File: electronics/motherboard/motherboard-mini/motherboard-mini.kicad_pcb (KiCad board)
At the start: 2 copper layers, 57.7 x 102.2 mm, 76 parts, among them J1 TBP02R2-381-03BE, J2 TBP02R2-381-02BE, J3 ST1W008S4AR1500, J4 TBP02R2-381-03BE, J5 USB4070-30-C_REVC5, J6 CONUFL001-SMD-T, J7 21992304, J8 Conn_01x04_Male, J9 TBP02R2-381-02BE, Q1 BSS214NW, Q2 AOD417, U1 MCP73832-2-OT, U2 NCP718xSN500, U3 INA219BxD, U4 LT3652IMSE, U6 INA219BxD, U7 LD39015M33R, U8 MIC2145BMM, U9 RFM95W-915S2

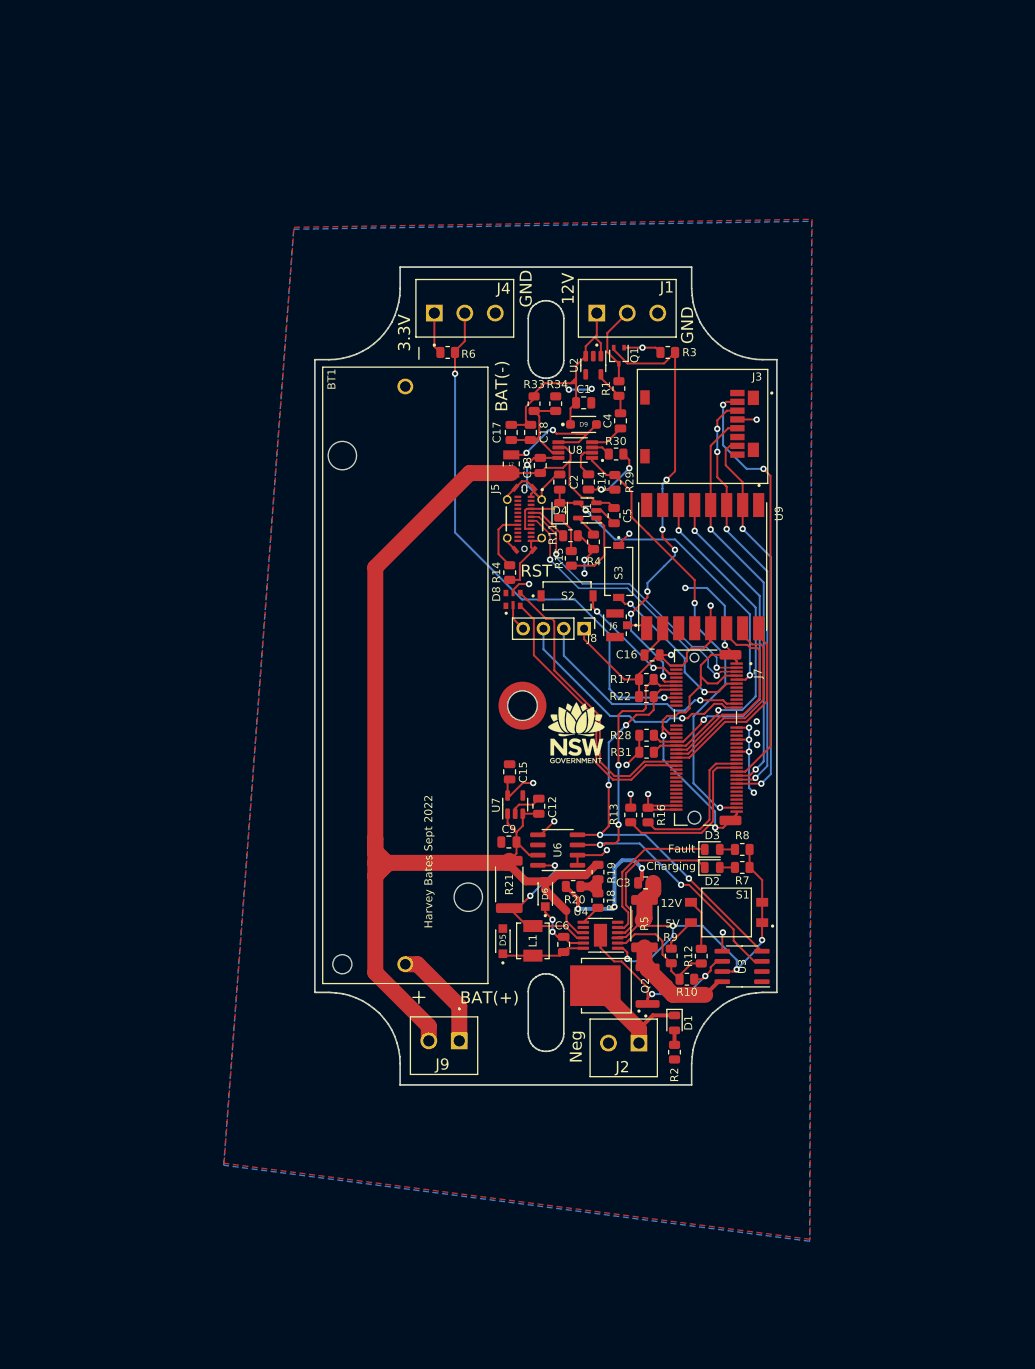
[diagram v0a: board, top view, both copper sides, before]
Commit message: realign with master branch before kangaroo board is split into seperate repo
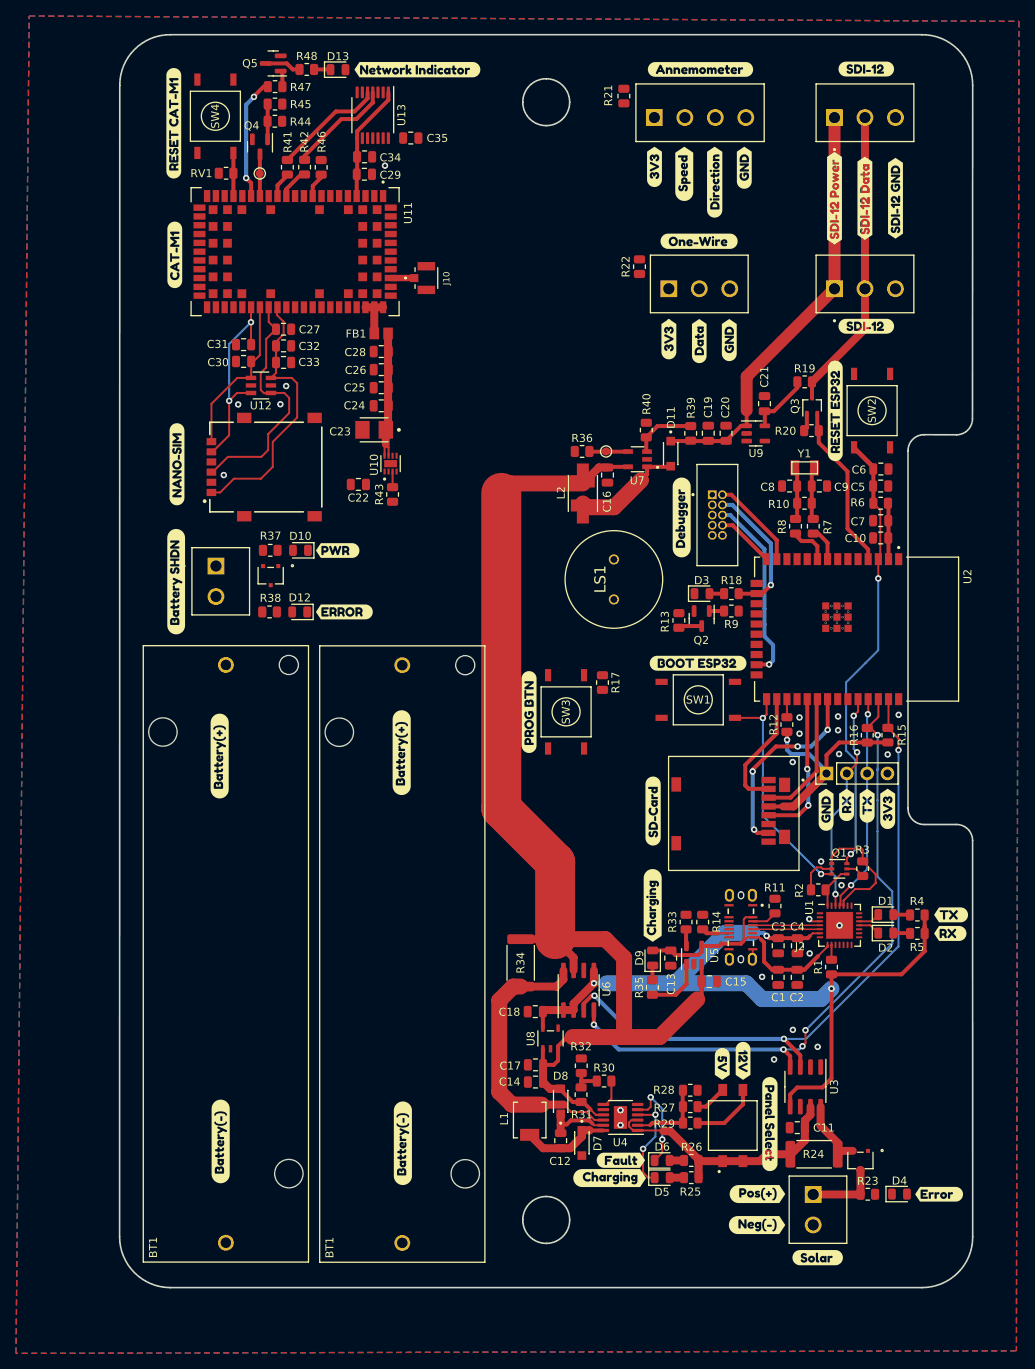
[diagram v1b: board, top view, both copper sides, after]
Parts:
- removed the BT1 at (67.7, 106.8)
- removed MP1: 9774025151R, 9774025151R:WE_9774025151R
- removed S2: RST, PTS636_SM43J_SMTR_LFS:SW_PTS636_SM43J_SMTR_LFS
- removed S3: BOOT, PTS636_SM43J_SMTR_LFS:SW_PTS636_SM43J_SMTR_LFS
- added BT1: 1043, 1043:BAT_1043, F.Cu at (45.3, 141.6)
- added BT1: 1043, 1043:BAT_1043, F.Cu at (67.3, 141.6)
- added C10: 22uF, Capacitor_SMD:C_0805_2012Metric, F.Cu at (127.1, 89.6)
- added C11: 10uF, Capacitor_SMD:C_0805_2012Metric, F.Cu at (116.7, 163.3)
- added C19: 10uF, Capacitor_SMD:C_0805_2012Metric, F.Cu at (105.6, 76.5)
- added C20: 1uF, Capacitor_SMD:C_0805_2012Metric, F.Cu at (107.8, 76.5)
- added C21: 1uF, Capacitor_SMD:C_0805_2012Metric, F.Cu at (112.6, 72.8)
- added C22: 1uF, Capacitor_SMD:C_0805_2012Metric, F.Cu at (61.8, 82.9)
- added C23: 100uF, T520B107M006ATE015:CAPPM3528X210N, F.Cu at (63.8, 76.1)
- added C24: 100nF, Capacitor_SMD:C_0805_2012Metric, F.Cu at (64.7, 73.1)
- added C25: 10nF, Capacitor_SMD:C_0805_2012Metric, F.Cu at (64.7, 70.8)
- added C26: 15pF, Capacitor_SMD:C_0805_2012Metric, F.Cu at (64.7, 68.5)
- added C27: 47pF, Capacitor_SMD:C_0805_2012Metric, F.Cu at (52.5, 63.5)
- added C28: 68pF, Capacitor_SMD:C_0805_2012Metric, F.Cu at (64.7, 66.3)
- added C29: 100nF, Capacitor_SMD:C_0805_2012Metric, F.Cu at (62.6, 44.1)
- added C30: 47pF, Capacitor_SMD:C_0805_2012Metric, F.Cu at (47.5, 67.5)
- added C31: 47pF, Capacitor_SMD:C_0805_2012Metric, F.Cu at (47.5, 65.4)
- added C32: 47pF, Capacitor_SMD:C_0805_2012Metric, F.Cu at (52.5, 65.6)
- added C33: 100nF, Capacitor_SMD:C_0805_2012Metric, F.Cu at (52.5, 67.7)
- added C34: 0.1uF, Capacitor_SMD:C_0805_2012Metric, F.Cu at (62.6, 42.0)
- added C35: 0.1uF, Capacitor_SMD:C_0805_2012Metric, F.Cu at (68.4, 39.6)
- added C7: 0.1uF, Capacitor_SMD:C_0805_2012Metric, F.Cu at (127.1, 87.4)
- added C8: 12pF, Capacitor_SMD:C_0805_2012Metric, F.Cu at (115.7, 83.1)
- added D10: LED(Green), LED_SMD:LED_0805_2012Metric, F.Cu at (54.6, 91.1)
- added D11: SS34LW_RVG, SS34LW_RVG:SODFL3718X102N, F.Cu at (100.9, 79.0)
- added D12: LED(Red), LED_SMD:LED_0805_2012Metric, F.Cu at (54.5, 98.8)
- added D13: LED, LED_SMD:LED_0805_2012Metric, F.Cu at (59.3, 31.1)
- added D7: SS34LW_RVG, SS34LW_RVG:SODFL3718X102N, F.Cu at (89.8, 165.2)
- added FB1: FBMH2012HM221-TV, FBMH2012HM221-TV:BEADC2012X105N, F.Cu at (64.7, 64.0)
- added J10: CONUFL001-SMD-T, CONUFL001-SMD-T:LINX_CONUFL001-SMD-T, F.Cu at (70.3, 57.1)
- added J11: SIM8060-6-0-14-00-A, SIM8060-6-0-14-00-A:GCT_SIM8060-6-0-14-00-A, F.Cu at (50.3, 80.7)
- added J12: JTAG, 3221-10-0100-00:CNC_3221-10-0100-00, F.Cu at (106.7, 86.7)
- added LS1: PS1240P02BT, PS1240P02BT:XDCR_PS1240P02BT, F.Cu at (93.8, 94.8)
- added MOSFET1: SSM3J340R_LF, SSM3J340R_LF:SSM3J340R_LF, F.Cu at (124.6, 167.4)
- added MOSFET2: SSM3J340R_LF, SSM3J340R_LF:SSM3J340R_LF, F.Cu at (50.9, 94.3)
- added Q3: BSS214NW, Package_TO_SOT_SMD:SOT-323_SC-70, F.Cu at (118.5, 73.0)
- added Q4: BC847, Package_TO_SOT_SMD:SOT-23, F.Cu at (49.5, 40.7)
- added Q5: BC847, Package_TO_SOT_SMD:SOT-23, F.Cu at (51.2, 30.3)
- added R23: 4.7K, Resistor_SMD:R_0805_2012Metric, F.Cu at (125.5, 171.6)
- added R24: 0.1, Resistor_SMD:R_2512_6332Metric, F.Cu at (118.8, 166.6)
- added R25: 4.7K, Resistor_SMD:R_0805_2012Metric, F.Cu at (103.5, 169.6)
- added R26: 4.7K, Resistor_SMD:R_0805_2012Metric, F.Cu at (103.5, 167.4)
- added R27: 23K, Resistor_SMD:R_0805_2012Metric, F.Cu at (103.3, 160.7)
- added R32: 330K, Resistor_SMD:R_0805_2012Metric, F.Cu at (89.7, 155.6)
- added R35: 1K, Resistor_SMD:R_0805_2012Metric, F.Cu at (98.6, 145.8)
- added R36: 100K, Resistor_SMD:R_0805_2012Metric, F.Cu at (89.8, 78.8)
- added R37: 4.7K, Resistor_SMD:R_0805_2012Metric, F.Cu at (50.8, 91.1)
- added R38: 4.7K, Resistor_SMD:R_0805_2012Metric, F.Cu at (50.7, 98.8)
- added R39: 43.3K, Resistor_SMD:R_0805_2012Metric, F.Cu at (103.4, 76.5)
- added R40: 5K, Resistor_SMD:R_0805_2012Metric, F.Cu at (97.8, 76.1)
- added R41: 0, Resistor_SMD:R_0805_2012Metric, F.Cu at (53.0, 43.2)
- added R42: 0, Resistor_SMD:R_0805_2012Metric, F.Cu at (55.1, 43.2)
- added R43: 100K, Resistor_SMD:R_0805_2012Metric, F.Cu at (66.1, 84.2)
- added R44: 10K, Resistor_SMD:R_0805_2012Metric, F.Cu at (51.4, 37.5)
- added R45: 47K, Resistor_SMD:R_0805_2012Metric, F.Cu at (51.4, 35.4)
- added R46: 0, Resistor_SMD:R_0805_2012Metric, F.Cu at (57.2, 43.3)
- added R47: 10K, Resistor_SMD:R_0805_2012Metric, F.Cu at (51.4, 33.2)
- added R48: 1.2K, Resistor_SMD:R_0805_2012Metric, F.Cu at (55.4, 31.0)
- added RV1: ESD_RST_IN, Resistor_SMD:R_0805_2012Metric, F.Cu at (45.3, 44.0)
- added SW1: BOOT, 1977223-6:1977223-6, F.Cu at (104.3, 109.8)
- added SW2: RESET, 1977223-6:1977223-6, F.Cu at (126.1, 73.7)
- added SW3: PROG_BTN, 1977223-6:1977223-6, F.Cu at (87.8, 111.3)
- added SW4: CAT_M1_RST, 1977223-6:1977223-6, F.Cu at (44.0, 36.9)
- added TP1: 12V_EN, TestPoint:TestPoint_Pad_D1.0mm, F.Cu at (92.8, 78.8)
- added TP4: PWR_ON, TestPoint:TestPoint_Pad_D1.0mm, F.Cu at (49.5, 44.0)
- added U10: TPS22967DSGR, TPS22967DSGR:SON50P200X200X80-9N, F.Cu at (65.9, 80.3)
- added U11: SARA-R410M-02B, SARA-R410M-02B:XCVR_SARA-R410M-02B, F.Cu at (53.9, 53.8)
- added U12: AOZ8904CIL, AOZ8904CIL:AOZ8904CIL, F.Cu at (49.7, 70.5)
- added U13: TXB0104PW, Package_SO:TSSOP-14_4.4x5mm_P0.65mm, F.Cu at (63.6, 36.8)
- added U5: MCP73832-2-OT, Package_TO_SOT_SMD:SOT-23-5, F.Cu at (103.8, 141.7)
- added Y1: 32.768KHz, ABS07AIG-32:XTAL320X150X90, F.Cu at (117.6, 80.8)
- added kibuzzard-635F8A2B: G***, kibuzzard-635F8A2B, F.Cu at (122.9, 123.0)
- added kibuzzard-635F8A68: G***, kibuzzard-635F8A68, F.Cu at (125.4, 123.1)
- added kibuzzard-635F8A75: G***, kibuzzard-635F8A75, F.Cu at (128.0, 123.5)
- added kibuzzard-635F8A8D: G***, kibuzzard-635F8A8D, F.Cu at (120.3, 123.6)
- added kibuzzard-635F8E2B: G***, kibuzzard-635F8E2B, F.Cu at (44.6, 165.0)
- added kibuzzard-635F8E2B: G***, kibuzzard-635F8E2B, F.Cu at (67.4, 165.2)
- added kibuzzard-635F8E59: G***, kibuzzard-635F8E59, F.Cu at (67.2, 116.4)
- added kibuzzard-635F8E59: G***, kibuzzard-635F8E59, F.Cu at (44.5, 116.8)
- added kibuzzard-635F905F: G***, kibuzzard-635F905F, F.Cu at (60.1, 98.8)
- added kibuzzard-635F906F: G***, kibuzzard-635F906F, F.Cu at (59.3, 91.2)
- added kibuzzard-635F91A1: G***, kibuzzard-635F91A1, F.Cu at (135.9, 136.7)
- added kibuzzard-635F91AE: G***, kibuzzard-635F91AE, F.Cu at (135.8, 139.0)
- added kibuzzard-635F9520: G***, kibuzzard-635F9520, F.Cu at (39.2, 80.4)
- added kibuzzard-635F9541: G***, kibuzzard-635F9541, F.Cu at (39.1, 95.0)
- added kibuzzard-635FAFDC: G***, kibuzzard-635FAFDC, F.Cu at (69.2, 31.1)
- added kibuzzard-635FB008: G***, kibuzzard-635FB008, F.Cu at (38.8, 37.8)
- added kibuzzard-635FB066: G***, kibuzzard-635FB066, F.Cu at (38.9, 54.2)
- added kibuzzard-635FB58D: G***, kibuzzard-635FB58D, F.Cu at (121.5, 73.7)
- added kibuzzard-635FB5EA: G***, kibuzzard-635FB5EA, F.Cu at (104.3, 105.2)
- added kibuzzard-63606B27: G***, kibuzzard-63606B27, F.Cu at (119.2, 179.6)
- added kibuzzard-63606B50: G***, kibuzzard-63606B50, F.Cu at (111.7, 171.6)
- added kibuzzard-63606B62: G***, kibuzzard-63606B62, F.Cu at (111.7, 175.5)
- added kibuzzard-63606B90: G***, kibuzzard-63606B90, F.Cu at (107.3, 155.3)
- added kibuzzard-63606BA0: G***, kibuzzard-63606BA0, F.Cu at (109.9, 154.9)
- added kibuzzard-63606BEB: G***, kibuzzard-63606BEB, F.Cu at (113.3, 162.8)
- added kibuzzard-63606C19: G***, kibuzzard-63606C19, F.Cu at (134.4, 171.6)
- added kibuzzard-63606D76: G***, kibuzzard-63606D76, F.Cu at (93.2, 169.6)
- added kibuzzard-63606D99: G***, kibuzzard-63606D99, F.Cu at (94.7, 167.4)
- added kibuzzard-6360750E: G***, kibuzzard-6360750E, F.Cu at (98.6, 135.5)
- added kibuzzard-636098FD: G***, kibuzzard-636098FD, F.Cu at (98.7, 123.7)
- added kibuzzard-6360A408: G***, kibuzzard-6360A408, F.Cu at (83.2, 111.3)
- added kibuzzard-6360A96B: G***, kibuzzard-6360A96B, F.Cu at (125.3, 63.1)
- added kibuzzard-6360A96B: G***, kibuzzard-6360A96B, F.Cu at (125.3, 31.0)
- added kibuzzard-6360B45A: G***, kibuzzard-6360B45A, F.Cu at (102.2, 87.0)
- added kibuzzard-6360B4B7: G***, kibuzzard-6360B4B7, F.Cu at (125.2, 47.1)
- added kibuzzard-6360B4C0: G***, kibuzzard-6360B4C0, F.Cu at (121.3, 47.1)
- added kibuzzard-6360B4D6: G***, kibuzzard-6360B4D6, F.Cu at (129.0, 47.1)
- added kibuzzard-6360B5B2: G***, kibuzzard-6360B5B2, F.Cu at (104.6, 31.0)
- added kibuzzard-6360B5D7: G***, kibuzzard-6360B5D7, F.Cu at (100.7, 64.7)
- added kibuzzard-6360B5D7: G***, kibuzzard-6360B5D7, F.Cu at (98.8, 43.2)
- added kibuzzard-6360B5FD: G***, kibuzzard-6360B5FD, F.Cu at (102.6, 44.1)
- added kibuzzard-6360B60D: G***, kibuzzard-6360B60D, F.Cu at (106.4, 45.1)
- added kibuzzard-6360B61D: G***, kibuzzard-6360B61D, F.Cu at (108.2, 64.8)
- added kibuzzard-6360B61D: G***, kibuzzard-6360B61D, F.Cu at (110.1, 43.3)
- added kibuzzard-6360B644: G***, kibuzzard-6360B644, F.Cu at (104.4, 52.5)
- added kibuzzard-6360B662: G***, kibuzzard-6360B662, F.Cu at (104.5, 65.0)
- C1, C15, C4: value 1uF -> 4.7uF
- C13: value 10uF -> 4.7uF
- C14: value 0.01uF -> 10uF
- C16: value 10uF -> 2.2uF
- C17: value 100pF -> 1uF
- C18: value 10uF -> 0.1
- C2: value 4.7uF -> 0.1uF
- C3: value 10uF -> 0.1uF
- C5: value 4.7uF -> 1uF
- C6: value 1uF -> 0.1uF
- C9: value 10uF -> 12pF
- D1: value LED(Red) -> LED(Orange)
- D2: value LED(Green) -> LED(Yellow)
- D3: value LED(Red) -> LED(Yellow)
- D4: value LED -> LED(Red)
- D5: value SS34LW_RVG -> LED(Green); footprint SS34LW_RVG:SODFL3718X102N -> LED_SMD:LED_0805_2012Metric
- D6: value SS34LW_RVG -> LED(Red); footprint SS34LW_RVG:SODFL3718X102N -> LED_SMD:LED_0805_2012Metric
- D8: value BB-2020BGR-TRB -> SS34LW_RVG; footprint BB-2020BGR-TRB:LED_BB-2020BGR-TRB -> SS34LW_RVG:SODFL3718X102N
- D9: value D_Schottky -> LED; footprint SM5817PL:SODFL3718X108N -> LED_SMD:LED_0805_2012Metric
- J1: value TBP02R2-381-03BE -> JTAG; footprint TBP02R2-381-03BE:CUI_TBP02R2-381-03BE -> Connector_PinHeader_2.54mm:PinHeader_1x04_P2.54mm_Vertical
- J2: value TBP02R2-381-02BE -> ST1W008S4AR1500; footprint TBP02R2-381-02BE:CUI_TBP02R2-381-02BE -> ST1W008S4AR1500:JAE_ST1W008S4AR1500
- J3: value ST1W008S4AR1500 -> TBP02R2-381-03BE; footprint ST1W008S4AR1500:JAE_ST1W008S4AR1500 -> TBP02R2-381-03BE:CUI_TBP02R2-381-03BE
- J5: footprint USB4070-30-C:USB4070-30-C -> USB4145-03-0230-C_REVA:GCT_USB4145-03-0230-C_REVA
- J6: value CONUFL001-SMD-T -> TBP02R2-381-04BE; footprint CONUFL001-SMD-T:LINX_CONUFL001-SMD-T -> TBP02R2-381-04BE:CUI_TBP02R2-381-04BE
- J7: value 21992304 -> TBP02R2-381-03BE; footprint 21992304:TE_21992304 -> TBP02R2-381-03BE:CUI_TBP02R2-381-03BE
- J8: value Conn_01x04_Male -> SOLAR_CONN; footprint Connector_PinHeader_2.54mm:PinHeader_1x04_P2.54mm_Vertical -> TBP02R2-381-02BE:CUI_TBP02R2-381-02BE
- J9: value TBP02R2-381-02BE -> BATT_SHDN
- L2: value CBC2518T100M -> LQH43CN100K03L; footprint CBC2518T100M:INDC2518X200N -> LQH43CN100K03L:IND_LQH43CN100K03L
- Q1: value BSS214NW -> MMDT3904; footprint Package_TO_SOT_SMD:SOT-323_SC-70 -> Package_TO_SOT_SMD:SOT-363_SC-70-6
- Q2: value AOD417 -> BC847; footprint AOD417:DPAK228P994X240_3N -> Package_TO_SOT_SMD:SOT-23
- R1: value 10K -> 1K
- R10: value 27K -> 10M
- R12: value 53.6K -> 10K
- R13: value 4.7K -> 1K
- R15: value 680 -> 4.7K
- R17, R2, R6: value 4.7K -> 10K
- R18: value 191K -> 2K
- R19: value 70K -> 10K
- R20: value 330K -> 10K
- R21: value 0.1 -> 4.7K; footprint Resistor_SMD:R_2512_6332Metric -> Resistor_SMD:R_0805_2012Metric
- R28: value 100K -> 27K
- R29: value 1M -> 53.6K
- R30: value 10K -> 180K
- R31: value 100K -> 91K
- R33: value 50K -> 3.2K
- R34: value 5K -> 0.1; footprint Resistor_SMD:R_0805_2012Metric -> Resistor_SMD:R_2512_6332Metric
- R4: value 3.2K -> 1K
- R5: value 0.1 -> 1K; footprint Resistor_SMD:R_2512_6332Metric -> Resistor_SMD:R_0805_2012Metric
- R7, R8: value 4.7K -> 0
- R9: value 23K -> 10K
- U1: value MCP73832-2-OT -> CP2102N-Axx-xQFN28; footprint Package_TO_SOT_SMD:SOT-23-5 -> Package_DFN_QFN:QFN-28-1EP_5x5mm_P0.5mm_EP3.35x3.35mm
- U2: value NCP718xSN500 -> ESP32-WROOM-32E_(16MB); footprint Package_TO_SOT_SMD:SOT-23-5 -> ESP32-WROOM-32E__16MB_:XCVR_ESP32-WROOM-32E_(16MB)
- U7: value LD39015M33R -> MIC2288YD5-TR; footprint Package_TO_SOT_SMD:SOT-23-5 -> MIC2288YD5-TR:SOT95P280X100-5N
- U8: value MIC2145BMM -> XC6215B332MR-G; footprint MIC2145BMM:MIC2145BMM -> XC6215B332:XC6215B332MR-G
- U9: value RFM95W-915S2 -> NCP718xSN500; footprint RFM95W-915S2:XCVR_RFM95W-915S2 -> Package_TO_SOT_SMD:SOT-23-5
- moved R21 99.6 mm to (95.0, 34.4), turned to -90 degrees
- moved D4 95.4 mm to (129.5, 171.6), turned to 0 degrees
- moved R29 80.6 mm to (103.3, 162.7), turned to 180 degrees
- moved C17 79.1 mm to (84.0, 155.4), turned to 180 degrees
- moved R30 78.4 mm to (92.5, 157.5), turned to 0 degrees
- moved R1 77.0 mm to (121.0, 143.2)
- moved J8 76.3 mm to (118.7, 171.7)
- moved C1 75.8 mm to (114.3, 144.5), turned to 90 degrees
- moved C14 75.3 mm to (84.0, 157.6), turned to 180 degrees
- moved U8 73.6 mm to (85.8, 152.2), turned to 90 degrees
- moved C18 72.4 mm to (84.0, 148.8), turned to 180 degrees
- moved C6 71.4 mm to (127.1, 81.0), turned to 0 degrees
- moved R34 70.0 mm to (82.1, 142.7), turned to 90 degrees
- moved Q1 69.8 mm to (122.0, 130.9), turned to 0 degrees
- moved C4 69.2 mm to (116.7, 140.6), turned to 90 degrees
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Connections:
- C1 pad 1: +12V -> GND
- C1 pad 2: GND -> VBUS
- C12 pad 1: VBAT -> Net-(C12-Pad1)
- C12 pad 2: GND -> Net-(C12-Pad2)
- C13 pad 1: VBAT -> VBUS
- C14 pad 1: Net-(C14-Pad1) -> VBAT
- C15 pad 1: +3.3V -> VBAT
- C16 pad 1: +3.3V -> VBAT
- C17 pad 1: +12V -> VBAT
- C17 pad 2: Net-(C17-Pad2) -> GND
- C18 pad 1: +12V -> +3.3V
- C18 pad 2: Net-(C17-Pad2) -> GND
- C2 pad 1: VBUS -> GND
- C2 pad 2: GND -> VBUS
- C3 pad 1: Net-(C3-Pad1) -> GND
- C3 pad 2: GND -> +3.3V
- C4 pad 1: +5VP -> GND
- C4 pad 2: GND -> +3.3V
- C5 pad 1: VBAT -> GND
- C5 pad 2: GND -> ESP_ENABLE
- C6 pad 1: Net-(C6-Pad1) -> ESP_ENABLE
- C6 pad 2: Net-(C6-Pad2) -> GND
- C9 pad 1: VBAT -> Net-(C9-Pad1)
- D3 pad 1: Net-(D3-Pad1) -> GND
- D4 pad 1: Net-(D4-Pad1) -> Net-(R23-Pad2)
- D4 pad 2: VBUS -> GND
- D9 pad 1: +12V -> Net-(D9-Pad1)
- D9 pad 2: Net-(D9-Pad2) -> VBUS
- J1 pad 1: +12V -> +3.3V
- J1 pad 2: Net-(J1-Pad2) -> UART_RX
- J1 pad 3: GND -> UART_TX
- J2 pad 1: Net-(D1-Pad1) -> unconnected-(J2-Pad1)
- J2 pad 2: GND -> GPIO4
- J3 pad 1: unconnected-(J3-Pad1) -> +12V
- J3 pad 2: SPI_CS -> Net-(J3-Pad2)
- J3 pad 3: SPI_MOSI -> GND
- J4 pad 1: +3.3V -> +12V
- J4 pad 2: D1 -> Net-(J3-Pad2)
- J6 pad 1: Net-(J6-Pad1) -> +3.3V
- J6 pad 2: GND -> GPIO39
- J6 pad 3: GND -> A2
- J7 pad 1: GND -> +3.3V
- J7 pad 2: +3.3V -> GPIO27
- J7 pad 3: USB_D+ -> GND
- J8 pad 1: +3.3V -> Net-(J8-Pad1)
- J8 pad 2: SWDCLK -> GND
- J9 pad 1: BAT(+) -> Net-(J9-Pad1)
- L1 pad 1: Net-(C6-Pad1) -> Net-(C12-Pad1)
- L2 pad 2: Net-(D9-Pad2) -> Net-(D11-PadA)
- Q1 pad 1: +3.3V -> UART_RTS
- Q1 pad 2: D0 -> Net-(Q1-Pad2)
- Q1 pad 3: Net-(J1-Pad2) -> GPIO0
- Q2 pad 1: GND -> Net-(R9-Pad2)
- Q2 pad 3: Net-(Q2-Pad3) -> Net-(LS1-Pad1)
- R1 pad 1: +5VP -> +3.3V
- R1 pad 2: Net-(J1-Pad2) -> Net-(R1-Pad2)
- R10 pad 1: Net-(R10-Pad1) -> Net-(C8-Pad1)
- R10 pad 2: GND -> Net-(C9-Pad1)
- R12 pad 1: Net-(R12-Pad1) -> +3.3V
- R12 pad 2: Net-(R10-Pad1) -> Net-(R12-Pad2)
- R13 pad 2: I2C_SCL1 -> Net-(LS1-Pad1)
- R15 pad 1: Net-(R15-Pad1) -> +3.3V
- R15 pad 2: Net-(D4-Pad1) -> I2C_SDA
- R16 pad 2: I2C_SDA1 -> I2C_SCL
- R17 pad 1: +3.3V -> GPIO17
- R17 pad 2: I2C_SDA -> GND
- R18 pad 1: Net-(R18-Pad1) -> GPIO13
- R18 pad 2: Net-(R18-Pad2) -> Net-(D3-Pad2)
- R19 pad 1: Net-(R18-Pad1) -> +5VP
- R19 pad 2: VBAT -> Net-(J3-Pad2)
- R2 pad 1: Net-(D1-Pad2) -> Net-(Q1-Pad2)
- R2 pad 2: GND -> UART_DTR
- R20 pad 1: GND -> +3.3V
- R20 pad 2: Net-(R18-Pad1) -> GPIO36
- R21 pad 1: Net-(L1-Pad2) -> GPIO39
- R21 pad 2: VBAT -> +3.3V
- R22 pad 1: +3.3V -> GPIO27
- R22 pad 2: I2C_SCL -> +3.3V
- R28 pad 1: GPIO0 -> Net-(R27-Pad2)
- R28 pad 2: +3.3V -> GND
- R29 pad 1: GND -> Net-(R29-Pad1)
- R29 pad 2: GPIO5 -> Net-(R27-Pad2)
- R3 pad 1: +3.3V -> Net-(Q1-Pad5)
- R3 pad 2: D0 -> UART_RTS
- R30 pad 1: GND -> Net-(R30-Pad1)
- R31 pad 1: GPIO1 -> Net-(R30-Pad1)
- R31 pad 2: +3.3V -> VBAT
- R33 pad 1: Net-(C17-Pad2) -> GND
- R33 pad 2: +12V -> Net-(R33-Pad2)
- R34 pad 1: GND -> Net-(L1-Pad2)
- R34 pad 2: Net-(C17-Pad2) -> VBAT
- R4 pad 1: GND -> +3.3V
- R4 pad 2: Net-(R4-Pad2) -> Net-(D1-Pad2)
- R5 pad 1: Net-(Q2-Pad3) -> Net-(D2-Pad2)
- R5 pad 2: Net-(C3-Pad1) -> +3.3V
- R6 pad 1: D1 -> +3.3V
- R6 pad 2: +3.3V -> ESP_ENABLE
- R7 pad 1: Net-(C3-Pad1) -> Net-(C9-Pad1)
- R7 pad 2: Net-(D2-Pad2) -> Net-(R7-Pad2)
- R8 pad 1: Net-(C3-Pad1) -> Net-(C8-Pad1)
- R8 pad 2: Net-(D3-Pad2) -> Net-(R8-Pad2)
- R9 pad 1: Net-(R9-Pad1) -> GPIO21
- R9 pad 2: Net-(R10-Pad1) -> Net-(R9-Pad2)
- S1 pad 1A: Net-(C3-Pad1) -> Net-(C11-Pad1)
- S1 pad 1B: Net-(R9-Pad1) -> Net-(R27-Pad1)
- S1 pad 2A: Net-(C3-Pad1) -> Net-(C11-Pad1)
- S1 pad 2B: Net-(R12-Pad1) -> Net-(R29-Pad1)
- U1 pad 1: Net-(R15-Pad1) -> unconnected-(U1-Pad1)
- U1 pad 2: GND -> unconnected-(U1-Pad2)
- U1 pad 3: VBAT -> GND
- U1 pad 4: VBUS -> USB_D+
- U1 pad 5: Net-(R4-Pad2) -> USB_D-
- U2 pad 1: +12V -> GND
- U2 pad 2: GND -> +3.3V
- U2 pad 3: +12V -> ESP_ENABLE
- U2 pad 4: unconnected-(U2-Pad4) -> GPIO36
- U2 pad 5: +5VP -> GPIO39
- U3 pad 7: Net-(C3-Pad1) -> Net-(C11-Pad1)
- U3 pad 8: Net-(Q2-Pad3) -> Net-(MOSFET1-Pad2)
- U4 pad 1: Net-(C3-Pad1) -> Net-(C11-Pad1)
- U4 pad 11: Net-(C6-Pad2) -> Net-(C12-Pad2)
- U4 pad 12: Net-(C6-Pad1) -> Net-(C12-Pad1)
- U4 pad 2: Net-(R10-Pad1) -> Net-(R27-Pad2)
- U4 pad 3: Net-(C3-Pad1) -> Net-(C11-Pad1)
- U4 pad 4: Net-(D2-Pad1) -> Net-(D5-Pad1)
- U4 pad 5: Net-(D3-Pad1) -> Net-(D6-Pad1)
- U4 pad 7: Net-(R18-Pad2) -> Net-(R30-Pad2)
- U7 pad 1: VBAT -> Net-(D11-PadA)
- U7 pad 3: VBAT -> Net-(R39-Pad1)
- U7 pad 4: unconnected-(U7-Pad4) -> GPIO2
- U7 pad 5: +3.3V -> VBAT
- U8 pad 1: GPIO5 -> VBAT
- U8 pad 2: Net-(C14-Pad1) -> GND
- U8 pad 3: Net-(R30-Pad2) -> VBAT
- U8 pad 4: GND -> unconnected-(U8-Pad4)
- U8 pad 5: Net-(D9-Pad2) -> +3.3V
- U9 pad 1: GND -> +12V
- U9 pad 2: SPI_MISO -> unconnected-(U9-Pad2)
- U9 pad 3: SPI_MOSI -> GPIO2
- U9 pad 4: SPI_SCK -> unconnected-(U9-Pad4)
- U9 pad 5: GPIO0 -> +5VP
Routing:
- net GND: track 184.8 -> 2.76 mm
- net D1: track 68.2 -> 0.00 mm, vias 2 -> 0
- net +3.3V: track 77.8 -> 140.7 mm, vias 12 -> 4
- net ESP_ENABLE: track 0.00 -> 59.5 mm, vias 0 -> 2
- net D0: track 57.1 -> 0.00 mm, vias 6 -> 0
- net GPIO5: track 56.5 -> 0.00 mm, vias 2 -> 0
- net Net-(C3-Pad1): track 54.5 -> 0.00 mm, vias 4 -> 0
- net SPI_CS: track 53.9 -> 0.00 mm, vias 2 -> 0
- net GPIO1: track 43.8 -> 0.00 mm, vias 2 -> 0
- net Net-(J3-Pad2): track 0.00 -> 37.8 mm
- net SPI_MOSI: track 53.4 -> 16.5 mm, vias 4 -> 0
- net PDM_CLK: track 36.7 -> 0.00 mm
- net PDM_DATA: track 35.2 -> 0.00 mm
- net Net-(C32-Pad1): track 0.00 -> 34.1 mm
- net Net-(C11-Pad1): track 0.00 -> 33.3 mm
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- added copper zone on B.Cu, net GND
- removed copper zone on B.Cu, net +3.3V
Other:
- board size 57.7 x 102.2 mm -> 106.6 x 156.6 mm
- board text removed: "12V"
- board text removed: "3.3V"
- board text removed: "5V"
- board text removed: "BAT(+)"
- board text removed: "BAT(-)"
- board text removed: "Charging"
- board text removed: "Fault"
- board text removed: "GND"
- board text removed: "Harvey Bates Sept 2022"
- board text removed: "Neg"
- board text removed: "RST"

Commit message: added mounting circuit board and updated motherboard for next itteration
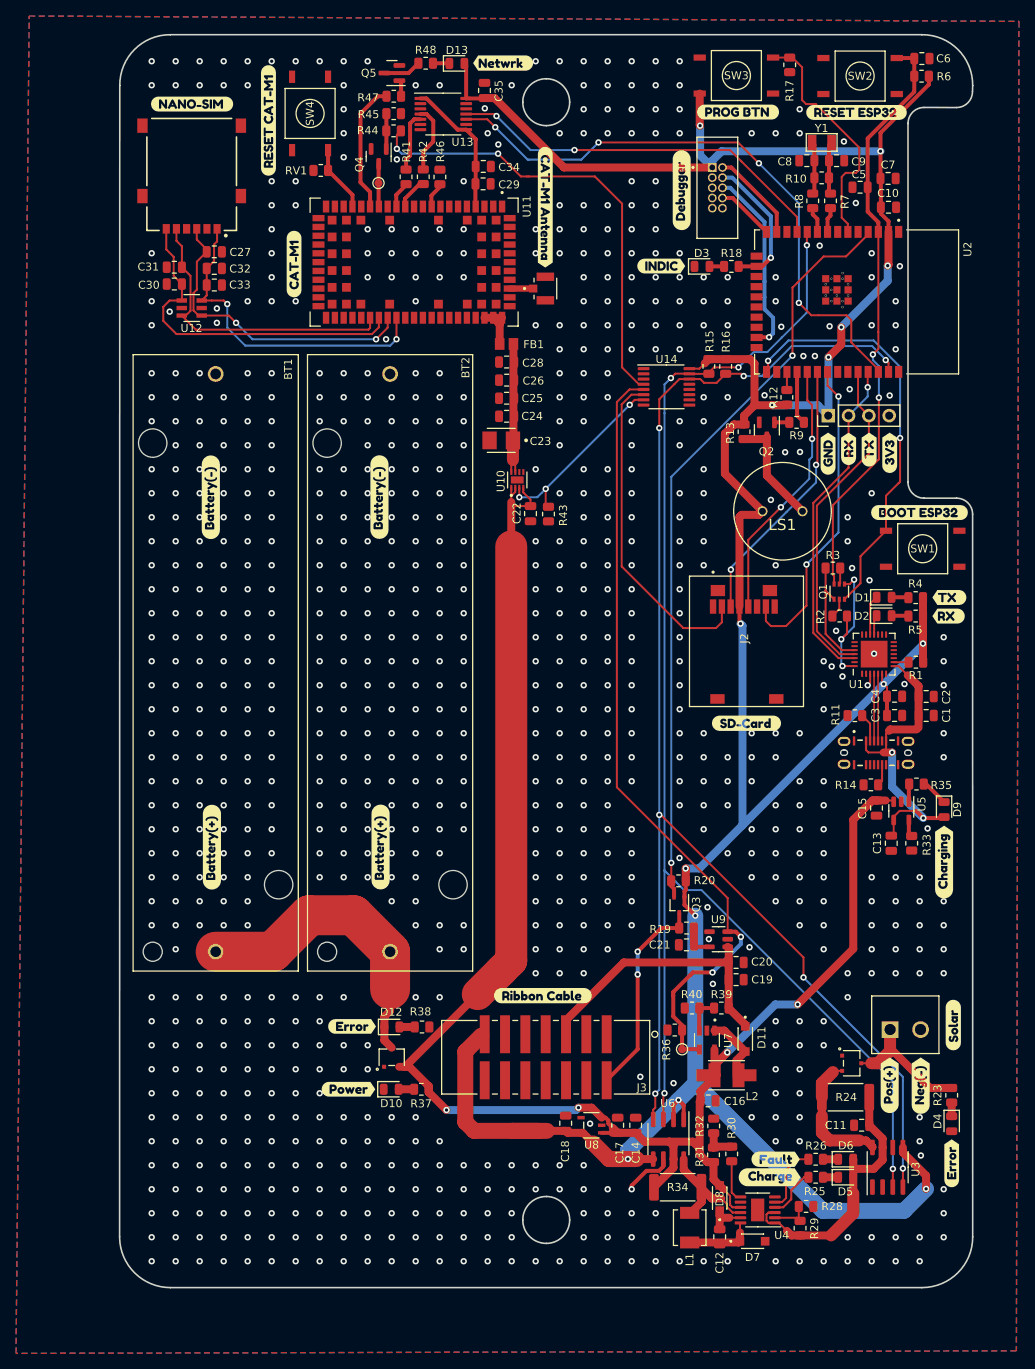
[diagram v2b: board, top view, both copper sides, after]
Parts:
- removed the BT1 at (67.3, 141.6)
- removed J4, J7: TBP02R2-381-03BE, TBP02R2-381-03BE:CUI_TBP02R2-381-03BE
- removed J6: TBP02R2-381-04BE, TBP02R2-381-04BE:CUI_TBP02R2-381-04BE
- removed J9: BATT_SHDN, TBP02R2-381-02BE:CUI_TBP02R2-381-02BE
- removed R21, R22: 4.7K, Resistor_SMD:R_0805_2012Metric
- removed R27: 23K, Resistor_SMD:R_0805_2012Metric
- removed S1: DS04-254-2-02BK-SMT, DS04-254-2-02BK-SMT:SW_DS04-254-2-02BK-SMT
- removed kibuzzard-635F905F: G***, kibuzzard-635F905F
- removed kibuzzard-635F906F: G***, kibuzzard-635F906F
- removed kibuzzard-635F9541: G***, kibuzzard-635F9541
- removed kibuzzard-635FAFDC: G***, kibuzzard-635FAFDC
- removed kibuzzard-63606B90: G***, kibuzzard-63606B90
- removed kibuzzard-63606BA0: G***, kibuzzard-63606BA0
- removed kibuzzard-63606BEB: G***, kibuzzard-63606BEB
- removed kibuzzard-63606C19: G***, kibuzzard-63606C19
- removed kibuzzard-63606D76: G***, kibuzzard-63606D76
- removed kibuzzard-6360750E: G***, kibuzzard-6360750E
- removed kibuzzard-6360A96B (x2): G***, kibuzzard-6360A96B
- removed kibuzzard-6360B4B7: G***, kibuzzard-6360B4B7
- removed kibuzzard-6360B4C0: G***, kibuzzard-6360B4C0
- removed kibuzzard-6360B4D6: G***, kibuzzard-6360B4D6
- removed kibuzzard-6360B5B2: G***, kibuzzard-6360B5B2
- removed kibuzzard-6360B5D7 (x2): G***, kibuzzard-6360B5D7
- removed kibuzzard-6360B5FD: G***, kibuzzard-6360B5FD
- removed kibuzzard-6360B60D: G***, kibuzzard-6360B60D
- removed kibuzzard-6360B61D (x2): G***, kibuzzard-6360B61D
- removed kibuzzard-6360B644: G***, kibuzzard-6360B644
- removed kibuzzard-6360B662: G***, kibuzzard-6360B662
- added BT2: 1043, 1043:BAT_1043, F.Cu at (65.8, 105.2)
- added U14: TCA9534, Package_SO:TSSOP-16_4.4x5mm_P0.65mm, F.Cu at (100.3, 70.7)
- added kibuzzard-6361FE78: G***, kibuzzard-6361FE78, F.Cu at (85.2, 48.2)
- added kibuzzard-63643555: G***, kibuzzard-63643555, F.Cu at (136.0, 167.8)
- added kibuzzard-63643CAA: G***, kibuzzard-63643CAA, F.Cu at (113.2, 169.5)
- added kibuzzard-636459CC: G***, kibuzzard-636459CC, F.Cu at (79.9, 30.2)
- added kibuzzard-6364627B: G***, kibuzzard-6364627B, F.Cu at (61.0, 150.7)
- added kibuzzard-636462B0: G***, kibuzzard-636462B0, F.Cu at (60.6, 158.5)
- added kibuzzard-6364640A: G***, kibuzzard-6364640A, F.Cu at (135.1, 130.1)
- added kibuzzard-63646461: G***, kibuzzard-63646461, F.Cu at (84.9, 146.8)
- added kibuzzard-63648775: G***, kibuzzard-63648775, F.Cu at (99.7, 55.6)
- J3: value TBP02R2-381-03BE -> 3020-14-0300-00; footprint TBP02R2-381-03BE:CUI_TBP02R2-381-03BE -> 3020-14-0300-00:3020-14-0300-00
- moved J3 122.9 mm to (85.2, 154.5), turned to 180 degrees
- moved SW3 82.3 mm to (109.1, 31.8), turned to 180 degrees
- moved kibuzzard-635F8E2B 80.8 mm to (64.5, 84.5)
- moved R17 80.7 mm to (115.8, 30.4)
- moved kibuzzard-635F8E2B 80.5 mm to (43.4, 84.5)
- moved kibuzzard-6360A408 79.4 mm to (109.3, 36.4), turned to 0 degrees
- moved C16 79.2 mm to (105.5, 159.9), turned to 0 degrees
- moved TP1 75.3 mm to (102.3, 153.5), turned to 0 degrees
- moved L2 74.9 mm to (107.8, 156.8), turned to 0 degrees
- moved D11 73.8 mm to (110.2, 152.2)
- moved R36 73.2 mm to (101.4, 151.1)
- moved U7 73.1 mm to (105.4, 152.3), turned to -90 degrees
- moved R40 72.5 mm to (103.5, 148.3), turned to 0 degrees
- moved R39 71.9 mm to (107.2, 148.3), turned to 0 degrees
- moved R37 70.0 mm to (69.7, 158.5), turned to 0 degrees
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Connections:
- net Net-(J3-Pad2) renamed SDI12_IN_OUT
- D5 pad 2: Net-(D5-Pad2) -> Net-(C11-Pad1)
- D6 pad 2: Net-(D6-Pad2) -> Net-(C11-Pad1)
- J1 pad 2: UART_RX -> UART_RX0
- J1 pad 3: UART_TX -> UART_TX0
- J2 pad 2: GPIO4 -> IO_P2
- J3 pad 1: +12V -> unconnected-(J3-Pad1)
- MOSFET2 pad 2: Net-(J9-Pad1) -> VBAT
- R17 pad 1: GPIO17 -> GPIO34
- R25 pad 1: Net-(C11-Pad1) -> Net-(D5-Pad1)
- R25 pad 2: Net-(D5-Pad2) -> Net-(R25-Pad2)
- R26 pad 1: Net-(C11-Pad1) -> Net-(D6-Pad1)
- R26 pad 2: Net-(D6-Pad2) -> Net-(R26-Pad2)
- R29 pad 1: Net-(R29-Pad1) -> Net-(C11-Pad1)
- R36 pad 2: GPIO2 -> IO_P1
- R37 pad 2: Net-(J9-Pad1) -> VBAT
- R43 pad 2: GPIO26 -> IO_P3
- R44 pad 1: GPIO25 -> IO_P0
- R9 pad 1: GPIO21 -> GPIO17
- SW2 pad 1: ESP_ENABLE -> unconnected-(SW2-Pad1)
- SW2 pad 2: unconnected-(SW2-Pad2) -> ESP_ENABLE
- SW2 pad 3: GND -> unconnected-(SW2-Pad3)
- SW2 pad 4: unconnected-(SW2-Pad4) -> GND
- SW3 pad 1: GPIO17 -> unconnected-(SW3-Pad1)
- SW3 pad 2: unconnected-(SW3-Pad2) -> GPIO34
- SW3 pad 3: +3.3V -> unconnected-(SW3-Pad3)
- SW3 pad 4: unconnected-(SW3-Pad4) -> +3.3V
- TP1 pad 1: GPIO2 -> IO_P1
- U1 pad 25: UART_TX -> UART_TX0
- U1 pad 26: UART_RX -> UART_RX0
- U10 pad 3: GPIO26 -> IO_P3
- U13 pad 10: UART_RX -> UART_TX1
- U13 pad 11: UART_TX -> UART_RX1
- U2 pad 10: GPIO25 -> I2C_SDA
- U2 pad 11: GPIO26 -> UART_RX1
- U2 pad 12: GPIO27 -> unconnected-(U2-Pad12)
- U2 pad 24: GPIO2 -> unconnected-(U2-Pad24)
- U2 pad 26: GPIO4 -> unconnected-(U2-Pad26)
- U2 pad 33: GPIO21 -> unconnected-(U2-Pad33)
- U2 pad 34: UART_RX -> UART_TX0
- U2 pad 35: UART_TX -> UART_RX0
- U2 pad 36: I2C_SCL -> UART_TX1
- U2 pad 37: I2C_SDA -> I2C_SCL
- U2 pad 5: GPIO39 -> unconnected-(U2-Pad5)
- U2 pad 6: A2 -> GPIO34
- U4 pad 4: Net-(D5-Pad1) -> Net-(R25-Pad2)
- U4 pad 5: Net-(D6-Pad1) -> Net-(R26-Pad2)
- U7 pad 4: GPIO2 -> IO_P1
- U9 pad 2: unconnected-(U9-Pad2) -> GND
- U9 pad 3: GPIO2 -> IO_P1
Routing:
- net +3.3V: track 140.7 -> 393.7 mm, vias 4 -> 14
- net I2C_SCL: track 82.3 -> 183.7 mm, vias 5 -> 7
- net IO_P1: track 0.00 -> 99.5 mm, vias 0 -> 2
- net I2C_SDA: track 83.6 -> 176.3 mm, vias 3 -> 5
- net UART_TX1: track 0.00 -> 75.5 mm, vias 0 -> 4
- net GPIO36: track 20.8 -> 95.1 mm, vias 0 -> 2
- net VBAT: track 146.8 -> 207.4 mm, vias 0 -> 4
- net IO_P0: track 0.00 -> 57.5 mm, vias 0 -> 2
- net UART_RX1: track 0.00 -> 48.6 mm, vias 0 -> 2
- net UART_RX0: track 0.00 -> 42.1 mm, vias 0 -> 1
- net UART_TX0: track 0.00 -> 41.6 mm
- net IO_P2: track 0.00 -> 41.5 mm
- net Net-(BT1-PadP): track 0.00 -> 38.2 mm
- net GPIO34: track 0.00 -> 30.4 mm
- net UART_RX: track 27.8 -> 0.00 mm, vias 3 -> 0
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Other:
- outline, holes or cut-outs redrawn

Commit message: first efforts with the new esp32 motherboard version
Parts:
- moved kibuzzard-635F8A75 7.75 mm to (120.5, 78.9)
- moved kibuzzard-635F8A8D 7.70 mm to (128.2, 79.0)
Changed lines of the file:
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@@
   )
   (footprint "kibuzzard-635F8A8D" (layer "F.Cu")
-    (at 120.55 79.05 90)
+    (at 128.25 79.05 90)
     (descr "Generated with KiBuzzard")
     (tags "kb_params=eyJBbGlnbm1lbnRDaG9pY2UiOiAiQ2VudGVyIiwgIkNhcExlZnRDaG9pY2UiOiAiKCIsICJDYXBSaWdodENob2ljZSI6ICI+IiwgIkZvbnRDb21ib0JveCI6ICJGcmVkb2thT25lIiwgIkhlaWdodEN0cmwiOiAiMSIsICJMYXllckNvbWJvQm94IjogIkYuU2lsa1MiLCAiTXVsdGlMaW5lVGV4dCI6ICJHTkQiLCAiUGFkZGluZ0JvdHRvbUN0cmwiOiAiNSIsICJQYWRkaW5nTGVmdEN0cmwiOiAiMSIsICJQYWRkaW5nUmlnaHRDdHJsIjogIjUiLCAiUGFkZGluZ1RvcEN0cmwiOiAiNSIsICJXaWR0aEN0cmwiOiAiMSJ9")
@@
   )
   (footprint "kibuzzard-635F8A75" (layer "F.Cu")
-    (at 128.25 78.94033 90)
+    (at 120.5 78.94033 90)
     (descr "Generated with KiBuzzard")
     (tags "kb_params=eyJBbGlnbm1lbnRDaG9pY2UiOiAiQ2VudGVyIiwgIkNhcExlZnRDaG9pY2UiOiAiKCIsICJDYXBSaWdodENob2ljZSI6ICI+IiwgIkZvbnRDb21ib0JveCI6ICJGcmVkb2thT25lIiwgIkhlaWdodEN0cmwiOiAiMSIsICJMYXllckNvbWJvQm94IjogIkYuU2lsa1MiLCAiTXVsdGlMaW5lVGV4dCI6ICIzVjMiLCAiUGFkZGluZ0JvdHRvbUN0cmwiOiAiNSIsICJQYWRkaW5nTGVmdEN0cmwiOiAiMSIsICJQYWRkaW5nUmlnaHRDdHJsIjogIjUiLCAiUGFkZGluZ1RvcEN0cmwiOiAiNSIsICJXaWR0aEN0cmwiOiAiMSJ9")
